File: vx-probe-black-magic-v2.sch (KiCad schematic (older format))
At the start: 31 parts, among them P1 USB MINI B, P2 +5v power input, P3 +5v external input, P4 CONN_02X05, P5 CONN_01X05, U1 stm32f070-qfp48, U2 AT45DB321D-SU, U3 TC1262-33VDB, Y1 8 MHz

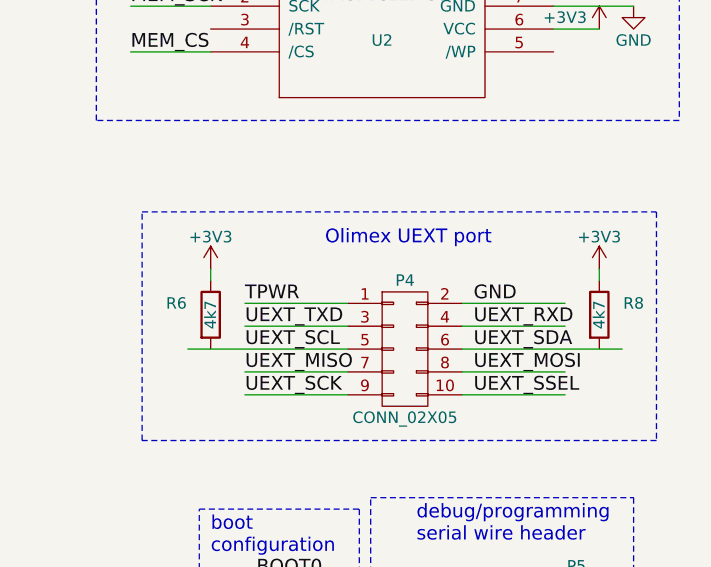
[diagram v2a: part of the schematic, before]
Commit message: added missing wires, started placing components
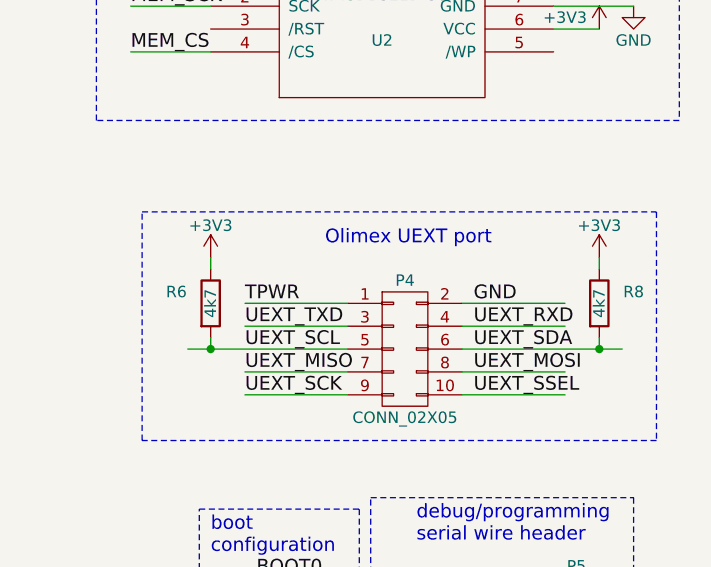
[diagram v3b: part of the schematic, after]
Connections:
- wire segments 102 -> 104
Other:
- moved on the sheet: R6, R8
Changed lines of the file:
@@
 L R R6
 U 1 1 57D8663E
-P 8950 2600
-F 0 "R6" H 8800 2650 50  0000 C CNN
-F 1 "4k7" V 8950 2600 50  0000 C CNN
-F 2 "Resistors_SMD:R_0805" V 8880 2600 50  0001 C CNN
-F 3 "" H 8950 2600 50  0000 C CNN
-	1    8950 2600
+P 8950 2550
+F 0 "R6" H 8800 2600 50  0000 C CNN
+F 1 "4k7" V 8950 2550 50  0000 C CNN
+F 2 "Resistors_SMD:R_0805" V 8880 2550 50  0001 C CNN
+F 3 "" H 8950 2550 50  0000 C CNN
+	1    8950 2550
 	1    0    0    -1
 $EndComp
@@
 L +3V3 #PWR09
 U 1 1 57D86D6F
-P 8950 2400
-F 0 "#PWR09" H 8950 2250 50  0001 C CNN
-F 1 "+3V3" H 8950 2540 50  0000 C CNN
-F 2 "" H 8950 2400 50  0000 C CNN
-F 3 "" H 8950 2400 50  0000 C CNN
-	1    8950 2400
+P 8950 2350
+F 0 "#PWR09" H 8950 2200 50  0001 C CNN
+F 1 "+3V3" H 8950 2490 50  0000 C CNN
+F 2 "" H 8950 2350 50  0000 C CNN
+F 3 "" H 8950 2350 50  0000 C CNN
+	1    8950 2350
 	1    0    0    -1
 $EndComp
@@
 L R R8
 U 1 1 57D86DD6
-P 10650 2600
-F 0 "R8" H 10800 2650 50  0000 C CNN
-F 1 "4k7" V 10650 2600 50  0000 C CNN
-F 2 "Resistors_SMD:R_0805" V 10580 2600 50  0001 C CNN
-F 3 "" H 10650 2600 50  0000 C CNN
-	1    10650 2600
+P 10650 2550
+F 0 "R8" H 10800 2600 50  0000 C CNN
+F 1 "4k7" V 10650 2550 50  0000 C CNN
+F 2 "Resistors_SMD:R_0805" V 10580 2550 50  0001 C CNN
+F 3 "" H 10650 2550 50  0000 C CNN
+	1    10650 2550
 	1    0    0    -1
 $EndComp
@@
 L +3V3 #PWR010
 U 1 1 57D86DDD
-P 10650 2400
-F 0 "#PWR010" H 10650 2250 50  0001 C CNN
-F 1 "+3V3" H 10650 2540 50  0000 C CNN
-F 2 "" H 10650 2400 50  0000 C CNN
-F 3 "" H 10650 2400 50  0000 C CNN
-	1    10650 2400
+P 10650 2350
+F 0 "#PWR010" H 10650 2200 50  0001 C CNN
+F 1 "+3V3" H 10650 2490 50  0000 C CNN
+F 2 "" H 10650 2350 50  0000 C CNN
+F 3 "" H 10650 2350 50  0000 C CNN
+	1    10650 2350
 	1    0    0    -1
 $EndComp
@@
 	9550 2950 9100 2950
 Wire Wire Line
-	8950 2450 8950 2400
-Wire Wire Line
-	10650 2450 10650 2400
+	8950 2400 8950 2350
+Wire Wire Line
+	10650 2400 10650 2350
 Wire Notes Line
 	8650 2150 10900 2150
@@
 Wire Notes Line
 	8400 6450 8400 5000
+Wire Wire Line
+	8950 2700 8950 2750
+Connection ~ 8950 2750
+Wire Wire Line
+	10650 2700 10650 2750
+Connection ~ 10650 2750
 $EndSCHEMATC

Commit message: started placing and routing the swdio/jtag connector
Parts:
- added P6: swdio/jtag, Pin_Headers:Pin_Header_Straight_2x05, symbol CONN_02X05
- added Q1: Q_PMOS_GSD, TO_SOT_Packages_SMD:SOT-23, symbol Q_PMOS_GSD
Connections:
- net labels added: SWCLK/TCK, SWDIO/TMS, SWO/TDO, TDI, TPWR_CTRL, XRST
- wire segments 104 -> 122
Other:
- note added: "Note: cut pin 7\nfor key"
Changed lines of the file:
@@
 	10650 2700 10650 2750
 Connection ~ 10650 2750
+$Comp
+L CONN_02X05 P6
+U 1 1 57D9507B
+P 5400 6900
+F 0 "P6" H 5400 7200 50  0000 C CNN
+F 1 "swdio/jtag" H 5400 7350 50  0000 C CNN
+F 2 "Pin_Headers:Pin_Header_Straight_2x05" H 5400 5700 50  0001 C CNN
+F 3 "" H 5400 5700 50  0000 C CNN
+	1    5400 6900
+	-1   0    0    -1
+$EndComp
+Wire Wire Line
+	5650 6700 5950 6700
+Wire Wire Line
+	5650 7100 6050 7100
+Wire Wire Line
+	5650 6800 6050 6800
+Wire Wire Line
+	4650 6700 5150 6700
+Text Label 5650 6700 0    60   ~ 0
+TPWR
+Wire Wire Line
+	6050 6800 6050 7300
+Connection ~ 6050 7100
+$Comp
+L GND #PWR020
+U 1 1 57D95865
+P 6050 7300
+F 0 "#PWR020" H 6050 7050 50  0001 C CNN
+F 1 "GND" H 6050 7150 50  0000 C CNN
+F 2 "" H 6050 7300 50  0000 C CNN
+F 3 "" H 6050 7300 50  0000 C CNN
+	1    6050 7300
+	1    0    0    -1
+$EndComp
+Text Label 4650 6700 0    60   ~ 0
+SWDIO/TMS
+Wire Wire Line
+	4650 6800 5150 6800
+Wire Wire Line
+	4650 6900 5150 6900
+Wire Wire Line
+	4650 7000 5150 7000
+Wire Wire Line
+	4650 7100 5150 7100
+Text Label 4650 6800 0    60   ~ 0
+SWCLK/TCK
+Text Label 4650 6900 0    60   ~ 0
+SWO/TDO
+Text Label 4650 7000 0    60   ~ 0
+TDI
+Text Label 4650 7100 0    60   ~ 0
+XRST
+Wire Wire Line
+	5650 6900 6050 6900
+Connection ~ 6050 6900
+Text Notes 5100 7400 0    60   ~ 0
+Note: cut pin 7\nfor key
+$Comp
+L Q_PMOS_GSD Q1
+U 1 1 57D96C39
+P 7450 6700
+F 0 "Q1" H 7750 6750 50  0000 R CNN
+F 1 "Q_PMOS_GSD" H 8100 6650 50  0000 R CNN
+F 2 "TO_SOT_Packages_SMD:SOT-23" H 7650 6800 50  0001 C CNN
+F 3 "" H 7450 6700 50  0000 C CNN
+	1    7450 6700
+	1    0    0    1
+$EndComp
+$Comp
+L +3V3 #PWR021
+U 1 1 57D96D1E
+P 7550 6400
+F 0 "#PWR021" H 7550 6250 50  0001 C CNN
+F 1 "+3V3" H 7550 6540 50  0000 C CNN
+F 2 "" H 7550 6400 50  0000 C CNN
+F 3 "" H 7550 6400 50  0000 C CNN
+	1    7550 6400
+	1    0    0    -1
+$EndComp
+Wire Wire Line
+	7550 6400 7550 6500
+Wire Wire Line
+	7550 6900 7550 7050
+Text Label 7550 7000 0    60   ~ 0
+TPWR
+Wire Wire Line
+	6850 6700 7250 6700
+Text Label 6850 6700 0    60   ~ 0
+TPWR_CTRL
+Wire Wire Line
+	6000 6150 6000 5650
+Text Label 6000 6150 1    60   ~ 0
+SWDIO/TMS
+Wire Wire Line
+	5900 6150 5900 5650
+Wire Wire Line
+	5800 6150 5800 5650
+Wire Wire Line
+	5700 6150 5700 5650
+Wire Wire Line
+	5600 6150 5600 5650
+Text Label 5900 6150 1    60   ~ 0
+SWCLK/TCK
+Text Label 5800 6150 1    60   ~ 0
+SWO/TDO
+Text Label 5700 6150 1    60   ~ 0
+TDI
+Text Label 5600 6150 1    60   ~ 0
+XRST
 $EndSCHEMATC

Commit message: routing optimizations
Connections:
- net labels added: USB_CONNECT
- wire segments 122 -> 125
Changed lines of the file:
@@
-	1    0    0    -1
-$EndComp
-$Comp
-L +3V3 #PWR015
-U 1 1 57D89E25
-P 1800 800
-F 0 "#PWR015" H 1800 650 50  0001 C CNN
-F 1 "+3V3" H 1800 940 50  0000 C CNN
-F 2 "" H 1800 800 50  0000 C CNN
-F 3 "" H 1800 800 50  0000 C CNN
-	1    1800 800
 	1    0    0    -1
 $EndComp
@@
 	2500 5200 2500 5250
 Wire Wire Line
-	4000 4050 3500 4050
-Wire Wire Line
-	3500 4050 3500 4850
-Wire Wire Line
-	3500 4850 2500 4850
+	3400 4050 4000 4050
 Wire Wire Line
 	3300 3750 3300 3850
@@
 TPWR_CTRL
 Wire Wire Line
+	5600 6150 5600 5650
+Text Label 5600 6150 1    60   ~ 0
+SWDIO/TMS
+Wire Wire Line
+	5700 6150 5700 5650
+Wire Wire Line
+	5800 5650 5800 6150
+Wire Wire Line
+	5900 6150 5900 5650
+Wire Wire Line
 	6000 6150 6000 5650
+Text Label 5700 6150 1    60   ~ 0
+SWCLK/TCK
+Text Label 5800 5750 3    60   ~ 0
+SWO/TDO
+Text Label 5900 6150 1    60   ~ 0
+TDI
 Text Label 6000 6150 1    60   ~ 0
-SWDIO/TMS
-Wire Wire Line
-	5900 6150 5900 5650
-Wire Wire Line
-	5800 6150 5800 5650
-Wire Wire Line
-	5700 6150 5700 5650
-Wire Wire Line
-	5600 6150 5600 5650
-Text Label 5900 6150 1    60   ~ 0
-SWCLK/TCK
-Text Label 5800 6150 1    60   ~ 0
-SWO/TDO
-Text Label 5700 6150 1    60   ~ 0
-TDI
-Text Label 5600 6150 1    60   ~ 0
 XRST
+Wire Wire Line
+	2500 4850 3400 4850
+Wire Wire Line
+	3400 4850 3400 4050
+Wire Wire Line
+	1800 800  1800 750
+Wire Wire Line
+	1800 750  2150 750
+Text Label 1800 750  0    60   ~ 0
+USB_CONNECT
+Wire Wire Line
+	7300 4150 7700 4150
+Text Label 7350 4150 0    60   ~ 0
+USB_CONNECT
 $EndSCHEMATC

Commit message: 11 vias
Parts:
- removed P5: CONN_01X05, Pin_Headers:Pin_Header_Straight_1x05, symbol CONN_01X05
- added P5: CONN_01X04, Pin_Headers:Pin_Header_Straight_1x04, symbol CONN_01X04
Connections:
- wire segments 125 -> 124
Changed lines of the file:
@@
 Text Label 6200 2250 1    60   ~ 0
 PROG_SWCLK
-$Comp
-L CONN_01X05 P5
-U 1 1 57D8BC7C
-P 10550 4000
-F 0 "P5" H 10550 4300 50  0000 C CNN
-F 1 "CONN_01X05" V 10650 4000 50  0000 C CNN
-F 2 "Pin_Headers:Pin_Header_Straight_1x05" H 10550 4000 50  0001 C CNN
-F 3 "" H 10550 4000 50  0000 C CNN
-	1    10550 4000
-	1    0    0    -1
-$EndComp
-Text Label 9800 3800 0    60   ~ 0
-5V_EXT
 Text Label 9800 3900 0    60   ~ 0
 GND
@@
 $EndComp
 $Comp
-L GND #PWR016
+L GND #PWR015
 U 1 1 57D8DA47
 P 9150 4100
-F 0 "#PWR016" H 9150 3850 50  0001 C CNN
+F 0 "#PWR015" H 9150 3850 50  0001 C CNN
 F 1 "GND" H 9150 3950 50  0000 C CNN
 F 2 "" H 9150 4100 50  0000 C CNN
@@
 +5V
 $Comp
-L GND #PWR017
+L GND #PWR016
 U 1 1 57D8EA04
 P 9950 5900
-F 0 "#PWR017" H 9950 5650 50  0001 C CNN
+F 0 "#PWR016" H 9950 5650 50  0001 C CNN
 F 1 "GND" H 9950 5750 50  0000 C CNN
 F 2 "" H 9950 5900 50  0000 C CNN
@@
 	6200 2350 6200 2150
 Wire Wire Line
-	9800 3800 10350 3800
-Wire Wire Line
 	9800 3900 10350 3900
 Wire Wire Line
@@
 Connection ~ 10450 5900
 $Comp
-L +3V3 #PWR018
+L +3V3 #PWR017
 U 1 1 57D8F462
 P 10750 5350
-F 0 "#PWR018" H 10750 5200 50  0001 C CNN
+F 0 "#PWR017" H 10750 5200 50  0001 C CNN
 F 1 "+3V3" H 10750 5490 50  0000 C CNN
 F 2 "" H 10750 5350 50  0000 C CNN
@@
 	9000 6250 9250 6250
 $Comp
-L GND #PWR019
+L GND #PWR018
 U 1 1 57D912A1
 P 9250 6250
-F 0 "#PWR019" H 9250 6000 50  0001 C CNN
+F 0 "#PWR018" H 9250 6000 50  0001 C CNN
 F 1 "GND" H 9250 6100 50  0000 C CNN
 F 2 "" H 9250 6250 50  0000 C CNN
@@
 Connection ~ 6050 7100
 $Comp
-L GND #PWR020
+L GND #PWR019
 U 1 1 57D95865
 P 6050 7300
-F 0 "#PWR020" H 6050 7050 50  0001 C CNN
+F 0 "#PWR019" H 6050 7050 50  0001 C CNN
 F 1 "GND" H 6050 7150 50  0000 C CNN
 F 2 "" H 6050 7300 50  0000 C CNN
@@
 $EndComp
 $Comp
-L +3V3 #PWR021
+L +3V3 #PWR020
 U 1 1 57D96D1E
 P 7550 6400
-F 0 "#PWR021" H 7550 6250 50  0001 C CNN
+F 0 "#PWR020" H 7550 6250 50  0001 C CNN
 F 1 "+3V3" H 7550 6540 50  0000 C CNN
 F 2 "" H 7550 6400 50  0000 C CNN
@@
 Text Label 7350 4150 0    60   ~ 0
 USB_CONNECT
+$Comp
+L CONN_01X04 P5
+U 1 1 57DA0126
+P 10550 4050
+F 0 "P5" H 10550 4300 50  0000 C CNN
+F 1 "CONN_01X04" V 10650 4050 50  0000 C CNN
+F 2 "Pin_Headers:Pin_Header_Straight_1x04" H 10550 4050 50  0001 C CNN
+F 3 "" H 10550 4050 50  0000 C CNN
+	1    10550 4050
+	1    0    0    -1
+$EndComp
 $EndSCHEMATC

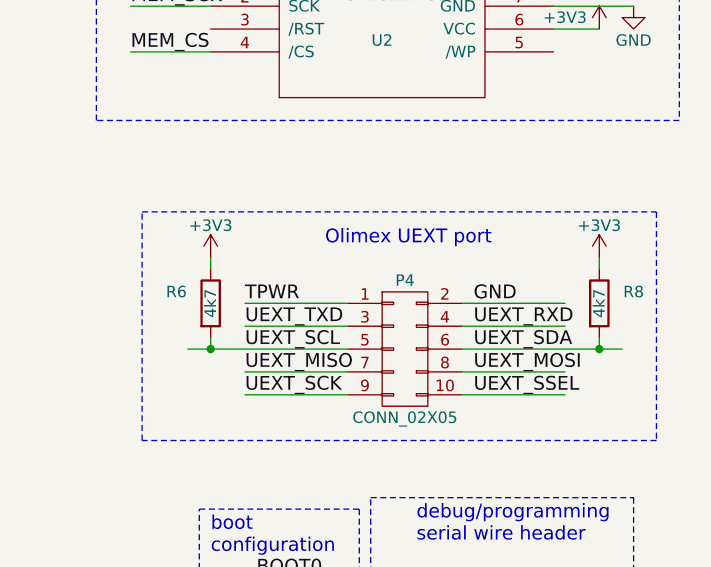
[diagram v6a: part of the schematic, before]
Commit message: removed i2c bus pull-up resistors
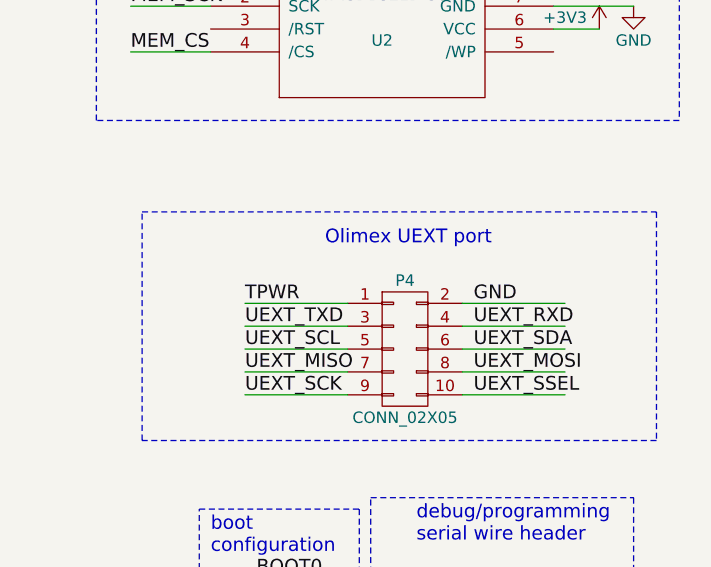
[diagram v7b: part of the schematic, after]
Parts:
- removed R6, R8: 4k7, Resistors_SMD:R_0805, symbol R
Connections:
- wire segments 124 -> 120
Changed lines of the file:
@@
 Text Label 10100 2950 0    60   ~ 0
 UEXT_SSEL
-$Comp
-L R R6
-U 1 1 57D8663E
-P 8950 2550
-F 0 "R6" H 8800 2600 50  0000 C CNN
-F 1 "4k7" V 8950 2550 50  0000 C CNN
-F 2 "Resistors_SMD:R_0805" V 8880 2550 50  0001 C CNN
-F 3 "" H 8950 2550 50  0000 C CNN
-	1    8950 2550
-	1    0    0    -1
-$EndComp
-$Comp
-L +3V3 #PWR09
-U 1 1 57D86D6F
-P 8950 2350
-F 0 "#PWR09" H 8950 2200 50  0001 C CNN
-F 1 "+3V3" H 8950 2490 50  0000 C CNN
-F 2 "" H 8950 2350 50  0000 C CNN
-F 3 "" H 8950 2350 50  0000 C CNN
-	1    8950 2350
-	1    0    0    -1
-$EndComp
-$Comp
-L R R8
-U 1 1 57D86DD6
-P 10650 2550
-F 0 "R8" H 10800 2600 50  0000 C CNN
-F 1 "4k7" V 10650 2550 50  0000 C CNN
-F 2 "Resistors_SMD:R_0805" V 10580 2550 50  0001 C CNN
-F 3 "" H 10650 2550 50  0000 C CNN
-	1    10650 2550
-	1    0    0    -1
-$EndComp
-$Comp
-L +3V3 #PWR010
-U 1 1 57D86DDD
-P 10650 2350
-F 0 "#PWR010" H 10650 2200 50  0001 C CNN
-F 1 "+3V3" H 10650 2490 50  0000 C CNN
-F 2 "" H 10650 2350 50  0000 C CNN
-F 3 "" H 10650 2350 50  0000 C CNN
-	1    10650 2350
-	1    0    0    -1
-$EndComp
 Text Notes 9450 2300 0    60   ~ 0
 Olimex UEXT port
@@
 $EndComp
 $Comp
-L GND #PWR011
+L GND #PWR09
 U 1 1 57D88BF4
 P 2700 7250
-F 0 "#PWR011" H 2700 7000 50  0001 C CNN
+F 0 "#PWR09" H 2700 7000 50  0001 C CNN
 F 1 "GND" H 2700 7100 50  0000 C CNN
 F 2 "" H 2700 7250 50  0000 C CNN
@@
 $EndComp
 $Comp
-L +3V3 #PWR012
+L +3V3 #PWR010
 U 1 1 57D88CB2
 P 2600 6800
-F 0 "#PWR012" H 2600 6650 50  0001 C CNN
+F 0 "#PWR010" H 2600 6650 50  0001 C CNN
 F 1 "+3V3" H 2600 6940 50  0000 C CNN
 F 2 "" H 2600 6800 50  0000 C CNN
@@
 $EndComp
 $Comp
-L GND #PWR013
+L GND #PWR011
 U 1 1 57D88FD9
 P 3200 7250
-F 0 "#PWR013" H 3200 7000 50  0001 C CNN
+F 0 "#PWR011" H 3200 7000 50  0001 C CNN
 F 1 "GND" H 3200 7100 50  0000 C CNN
 F 2 "" H 3200 7250 50  0000 C CNN
@@
 $EndComp
 $Comp
-L +3V3 #PWR014
+L +3V3 #PWR012
 U 1 1 57D890F4
 P 3200 6800
-F 0 "#PWR014" H 3200 6650 50  0001 C CNN
+F 0 "#PWR012" H 3200 6650 50  0001 C CNN
 F 1 "+3V3" H 3200 6940 50  0000 C CNN
 F 2 "" H 3200 6800 50  0000 C CNN
@@
 $EndComp
 $Comp
-L GND #PWR015
+L GND #PWR013
 U 1 1 57D8DA47
 P 9150 4100
-F 0 "#PWR015" H 9150 3850 50  0001 C CNN
+F 0 "#PWR013" H 9150 3850 50  0001 C CNN
 F 1 "GND" H 9150 3950 50  0000 C CNN
 F 2 "" H 9150 4100 50  0000 C CNN
@@
 +5V
 $Comp
-L GND #PWR016
+L GND #PWR014
 U 1 1 57D8EA04
 P 9950 5900
-F 0 "#PWR016" H 9950 5650 50  0001 C CNN
+F 0 "#PWR014" H 9950 5650 50  0001 C CNN
 F 1 "GND" H 9950 5750 50  0000 C CNN
 F 2 "" H 9950 5900 50  0000 C CNN
@@
 	10500 2650 10050 2650
 Wire Wire Line
-	10050 2750 10750 2750
-Wire Wire Line
 	10500 2850 10050 2850
 Wire Wire Line
@@
 	9550 2650 9100 2650
 Wire Wire Line
-	8850 2750 9550 2750
-Wire Wire Line
 	9550 2850 9100 2850
 Wire Wire Line
 	9550 2950 9100 2950
-Wire Wire Line
-	8950 2400 8950 2350
-Wire Wire Line
-	10650 2400 10650 2350
 Wire Notes Line
 	8650 2150 10900 2150
@@
 Connection ~ 10450 5900
 $Comp
-L +3V3 #PWR017
+L +3V3 #PWR015
 U 1 1 57D8F462
 P 10750 5350
-F 0 "#PWR017" H 10750 5200 50  0001 C CNN
+F 0 "#PWR015" H 10750 5200 50  0001 C CNN
 F 1 "+3V3" H 10750 5490 50  0000 C CNN
 F 2 "" H 10750 5350 50  0000 C CNN
@@
 	9000 6250 9250 6250
 $Comp
-L GND #PWR018
+L GND #PWR016
 U 1 1 57D912A1
 P 9250 6250
-F 0 "#PWR018" H 9250 6000 50  0001 C CNN
+F 0 "#PWR016" H 9250 6000 50  0001 C CNN
 F 1 "GND" H 9250 6100 50  0000 C CNN
 F 2 "" H 9250 6250 50  0000 C CNN
@@
 Wire Notes Line
 	8400 6450 8400 5000
-Wire Wire Line
-	8950 2700 8950 2750
-Connection ~ 8950 2750
-Wire Wire Line
-	10650 2700 10650 2750
-Connection ~ 10650 2750
 $Comp
 L CONN_02X05 P6
@@
 Connection ~ 6050 7100
 $Comp
-L GND #PWR019
+L GND #PWR017
 U 1 1 57D95865
 P 6050 7300
-F 0 "#PWR019" H 6050 7050 50  0001 C CNN
+F 0 "#PWR017" H 6050 7050 50  0001 C CNN
 F 1 "GND" H 6050 7150 50  0000 C CNN
 F 2 "" H 6050 7300 50  0000 C CNN
@@
 $EndComp
 $Comp
-L +3V3 #PWR020
+L +3V3 #PWR018
 U 1 1 57D96D1E
 P 7550 6400
-F 0 "#PWR020" H 7550 6250 50  0001 C CNN
+F 0 "#PWR018" H 7550 6250 50  0001 C CNN
 F 1 "+3V3" H 7550 6540 50  0000 C CNN
 F 2 "" H 7550 6400 50  0000 C CNN
@@
 	1    0    0    -1
 $EndComp
+Wire Wire Line
+	10050 2750 10500 2750
+Wire Wire Line
+	9550 2750 9100 2750
 $EndSCHEMATC

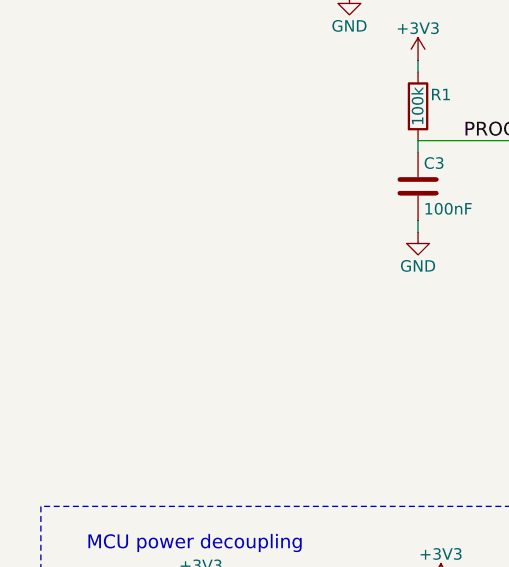
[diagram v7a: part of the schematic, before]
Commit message: adding dummy keep-off areas
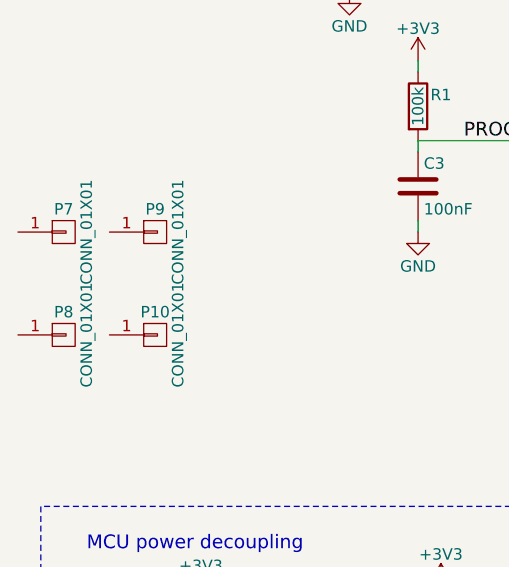
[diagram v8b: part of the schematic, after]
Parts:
- added P10, P7, P8, P9: CONN_01X01, Pin_Headers:Pin_Header_Straight_1x01, symbol CONN_01X01
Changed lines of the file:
@@
 Wire Wire Line
 	9550 2750 9100 2750
+$Comp
+L CONN_01X01 P8
+U 1 1 57DA9F25
+P 950 5700
+F 0 "P8" H 950 5800 50  0000 C CNN
+F 1 "CONN_01X01" V 1050 5700 50  0000 C CNN
+F 2 "Pin_Headers:Pin_Header_Straight_1x01" H 950 5700 50  0001 C CNN
+F 3 "" H 950 5700 50  0000 C CNN
+	1    950  5700
+	1    0    0    -1
+$EndComp
+$Comp
+L CONN_01X01 P10
+U 1 1 57DA9F2B
+P 1350 5700
+F 0 "P10" H 1350 5800 50  0000 C CNN
+F 1 "CONN_01X01" V 1450 5700 50  0000 C CNN
+F 2 "Pin_Headers:Pin_Header_Straight_1x01" H 1350 5700 50  0001 C CNN
+F 3 "" H 1350 5700 50  0000 C CNN
+	1    1350 5700
+	1    0    0    -1
+$EndComp
+$Comp
+L CONN_01X01 P7
+U 1 1 57DA9F78
+P 950 5250
+F 0 "P7" H 950 5350 50  0000 C CNN
+F 1 "CONN_01X01" V 1050 5250 50  0000 C CNN
+F 2 "Pin_Headers:Pin_Header_Straight_1x01" H 950 5250 50  0001 C CNN
+F 3 "" H 950 5250 50  0000 C CNN
+	1    950  5250
+	1    0    0    -1
+$EndComp
+$Comp
+L CONN_01X01 P9
+U 1 1 57DA9F7E
+P 1350 5250
+F 0 "P9" H 1350 5350 50  0000 C CNN
+F 1 "CONN_01X01" V 1450 5250 50  0000 C CNN
+F 2 "Pin_Headers:Pin_Header_Straight_1x01" H 1350 5250 50  0001 C CNN
+F 3 "" H 1350 5250 50  0000 C CNN
+	1    1350 5250
+	1    0    0    -1
+$EndComp
 $EndSCHEMATC
